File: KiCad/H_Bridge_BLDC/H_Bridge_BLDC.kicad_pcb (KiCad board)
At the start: 2 copper layers, 98 parts, among them J1 DriveCoil, J2 HallDec, J3 Ctrl, J4 12V, Q1 BC32740BU, Q10 BC33740BU, Q11 BC33740BU, Q12 BC33740BU, Q13 BC33740BU, Q14 BC33740BU, Q15 BC33740BU, Q16 BC33740BU, Q17 BC33740BU, Q2 TIP2955G, Q3 TIP3055G, Q4 TIP3055G, Q5 TIP2955G, Q6 BC32740BU, Q9 BC33740BU, U1 VO615A, U2 L7805CV, U3 CD74HC238E, U4 VO615A, U6 LM555xM, U7 LM555xM

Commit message: First version
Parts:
- added C16: 100n, Capacitor_THT:C_Disc_D4.7mm_W2.5mm_P5.00mm, F.Cu at (179.1, 150.4)
- added D18: ZY24 24V / 2W, Diode_THT:D_DO-41_SOD81_P10.16mm_Horizontal, F.Cu at (251.7, 174.3)
- added D19: 20V 1N5250B, Diode_THT:D_DO-35_SOD27_P10.16mm_Horizontal, F.Cu at (239.8, 153.8)
- added D20: 1N5408, Diode_THT:D_DO-201AD_P15.24mm_Horizontal, F.Cu at (243.8, 107.1)
- added D21: 1N5408, Diode_THT:D_DO-201AD_P15.24mm_Horizontal, F.Cu at (233.3, 85.4)
- added D22: 1N5408, Diode_THT:D_DO-201AD_P15.24mm_Horizontal, F.Cu at (239.8, 127.1)
- added D23: 1N5408, Diode_THT:D_DO-201AD_P15.24mm_Horizontal, F.Cu at (256.2, 122.0)
- added D24: LED, LED_THT:LED_D5.0mm, F.Cu at (183.5, 235.1)
- added D25: LED, LED_THT:LED_D5.0mm, F.Cu at (175.8, 235.3)
- added J5: Hall In, Connector_PinHeader_2.54mm:PinHeader_1x05_P2.54mm_Vertical, F.Cu at (171.3, 194.2)
- added J6: Hall Out, Connector_PinHeader_2.54mm:PinHeader_1x03_P2.54mm_Vertical, F.Cu at (196.5, 189.2)
- added Q18: 2N5401, Package_TO_SOT_THT:TO-92_Inline, F.Cu at (177.0, 213.7)
- added Q7: 2N5401, Package_TO_SOT_THT:TO-92_Inline, F.Cu at (192.5, 213.5)
- added Q8: 2N5401, Package_TO_SOT_THT:TO-92_Inline, F.Cu at (184.8, 213.6)
- added R12: 10k, Resistor_THT:R_Axial_DIN0207_L6.3mm_D2.5mm_P10.16mm_Horizontal, F.Cu at (237.5, 178.2)
- added R13: 2k2, Resistor_THT:R_Axial_DIN0207_L6.3mm_D2.5mm_P10.16mm_Horizontal, F.Cu at (229.8, 181.2)
- added R14: 1k, Resistor_THT:R_Axial_DIN0207_L6.3mm_D2.5mm_P10.16mm_Horizontal, F.Cu at (229.8, 157.3)
- added R15: 550, Resistor_THT:R_Axial_DIN0207_L6.3mm_D2.5mm_P10.16mm_Horizontal, F.Cu at (175.4, 193.5)
- added R16: 47, Resistor_THT:R_Axial_DIN0207_L6.3mm_D2.5mm_P10.16mm_Horizontal, F.Cu at (191.3, 207.8)
- added R42: 550, Resistor_THT:R_Axial_DIN0207_L6.3mm_D2.5mm_P10.16mm_Horizontal, F.Cu at (175.3, 189.2)
- added R43: 47, Resistor_THT:R_Axial_DIN0207_L6.3mm_D2.5mm_P10.16mm_Horizontal, F.Cu at (183.5, 207.8)
- added R44: 330, Resistor_THT:R_Axial_DIN0207_L6.3mm_D2.5mm_P10.16mm_Horizontal, F.Cu at (183.5, 218.5)
- added R45: 550, Resistor_THT:R_Axial_DIN0207_L6.3mm_D2.5mm_P10.16mm_Horizontal, F.Cu at (175.4, 185.0)
- added R46: 47, Resistor_THT:R_Axial_DIN0207_L6.3mm_D2.5mm_P10.16mm_Horizontal, F.Cu at (175.8, 207.8)
- added R47: 330, Resistor_THT:R_Axial_DIN0207_L6.3mm_D2.5mm_P10.16mm_Horizontal, F.Cu at (175.8, 218.7)
- added REF**: PinHeader_2x15_P2.54mm_Vertical, Connector_PinHeader_2.54mm:PinHeader_2x15_P2.54mm_Vertical, F.Cu at (249.5, 78.5)
- added REF**: PinHeader_2x15_P2.54mm_Vertical, Connector_PinHeader_2.54mm:PinHeader_2x15_P2.54mm_Vertical, F.Cu at (256.4, 78.5)
- added REF**: PinHeader_2x15_P2.54mm_Vertical, Connector_PinHeader_2.54mm:PinHeader_2x15_P2.54mm_Vertical, F.Cu at (263.3, 78.5)
- added REF**: PinHeader_2x15_P2.54mm_Vertical, Connector_PinHeader_2.54mm:PinHeader_2x15_P2.54mm_Vertical, F.Cu at (242.4, 78.5)
- C12: value 470uF 250V -> 100n; footprint footprints:CP_Radial_D25.0mm_P10.00mm_and_5mm -> Capacitor_THT:C_Disc_D4.7mm_W2.5mm_P5.00mm
- C3: footprint Capacitor_THT:CP_Radial_D25.0mm_P10.00mm_SnapIn -> Capacitor_THT:CP_Radial_D10.0mm_P5.00mm
- C4, C5, C6: footprint footprints:CP_Radial_D25.0mm_P10.00mm_and_5mm -> Capacitor_THT:CP_Radial_D10.0mm_P5.00mm
- D1: value GBU6B -> LED; footprint Diode_THT:Diode_Bridge_Vishay_GBU -> LED_THT:LED_D5.0mm
- Q1, Q6: value BC32740BU -> 2N5401
- Q10, Q11, Q12, Q13, Q14, Q15, Q16, Q17, Q9: value BC33740BU -> 2N5551
- Q2, Q5: value TIP2955G -> BDW94C; footprint Package_TO_SOT_THT:TO-247-3_Vertical -> Package_TO_SOT_THT:TO-220-3_Vertical
- Q3, Q4: value TIP3055G -> BDW93C; footprint Package_TO_SOT_THT:TO-247-3_Vertical -> Package_TO_SOT_THT:TO-220-3_Vertical
- U3: footprint footprints:N0016A -> Package_DIP:DIP-16_W7.62mm_LongPads
- moved R24 198.4 mm to (222.2, 167.5), turned to 90 degrees
- moved R27 184.8 mm to (222.0, 174.0), turned to 180 degrees
- moved Q13 183.5 mm to (231.3, 213.6), turned to 180 degrees
- moved Q12 183.5 mm to (238.8, 213.5), turned to 180 degrees
- moved Q14 183.0 mm to (223.3, 213.5), turned to 180 degrees
- moved Q15 182.5 mm to (215.8, 213.6), turned to 180 degrees
- moved R28 181.2 mm to (237.5, 197.3)
- moved Q16 181.1 mm to (207.9, 213.5), turned to 180 degrees
- moved R30 180.9 mm to (229.8, 197.3)
- moved Q17 180.9 mm to (200.2, 213.5), turned to 180 degrees
- moved R32 180.7 mm to (222.0, 197.3)
- moved R29 180.6 mm to (237.5, 228.7)
- moved R31 180.6 mm to (230.0, 228.7)
- moved D12 180.6 mm to (237.5, 232.6)
- moved D13 180.6 mm to (230.0, 232.6)
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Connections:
- C12 pad 1: +12V -> GNDD
- C12 pad 2: GND -> +5V
- D1 pad 1: /BR+ -> GNDD
- D1 pad 2: /C1 -> Net-(D1-A)
- D10 pad 1: Net-(D10-K) -> HALL_ENABLE
- D10 pad 2: unconnected-(D10-A-Pad2) -> Net-(D10-A)
- Q1 pad 1: Net-(Q1-C) -> Net-(Q1-E)
- Q1 pad 3: Net-(Q1-E) -> Net-(Q1-C)
- Q10 pad 1: HALL_ENABLE -> GNDD
- Q10 pad 2: unconnected-(Q10-B-Pad2) -> Net-(Q10-B)
- Q10 pad 3: GNDD -> HALL_ENABLE
- Q11 pad 1: Net-(Q11-C) -> GNDD
- Q11 pad 3: GNDD -> Net-(Q11-C)
- Q12 pad 1: Net-(Q12-C) -> GNDD
- Q12 pad 3: GNDD -> Net-(Q12-C)
- Q13 pad 1: Net-(Q13-C) -> GNDD
- Q13 pad 3: GNDD -> Net-(Q13-C)
- Q14 pad 1: Net-(Q14-C) -> GNDD
- Q14 pad 3: GNDD -> Net-(Q14-C)
- Q15 pad 1: Net-(Q15-C) -> GNDD
- Q15 pad 3: GNDD -> Net-(Q15-C)
- Q16 pad 1: Net-(Q16-C) -> GNDD
- Q16 pad 3: GNDD -> Net-(Q16-C)
- Q17 pad 1: Net-(Q17-C) -> GNDD
- Q17 pad 3: GNDD -> Net-(Q17-C)
- Q6 pad 1: Net-(Q4-B) -> Net-(Q6-E)
- Q6 pad 3: Net-(Q6-E) -> Net-(Q4-B)
- Q9 pad 1: Net-(Q9-C) -> GNDD
- Q9 pad 3: GNDD -> Net-(Q9-C)
- R22 pad 1: Net-(D10-K) -> HALL_1
- R22 pad 2: unconnected-(R22-Pad2) -> Net-(D1-A)
- U3 pad 1: unconnected-(U3-A0-Pad1) -> HALL_1
- U3 pad 2: unconnected-(U3-A1-Pad2) -> HALL_2
- U3 pad 3: unconnected-(U3-A2-Pad3) -> HALL_3
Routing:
- net +5V: track 74.6 -> 374.5 mm
- net /BR+: track 0.00 -> 108.1 mm
- net /C1: track 0.00 -> 108.1 mm
- net +12V: track 21.4 -> 125.3 mm
- net /C2: track 0.00 -> 97.5 mm
- net A: track 0.00 -> 83.9 mm, vias 0 -> 2
- net HALL_ENABLE: track 0.00 -> 79.6 mm, vias 0 -> 1
- net B: track 0.00 -> 62.8 mm, vias 0 -> 2
- net HALL_3: track 0.00 -> 59.8 mm
- net /PowerSupply/VD: track 40.0 -> 98.0 mm
- net HALL_2: track 0.00 -> 53.7 mm
- net HALL_1: track 0.00 -> 51.5 mm
- net /CAP_BANK: track 0.00 -> 43.3 mm
- net /SINGLE_CAP: track 0.00 -> 39.8 mm
- net Net-(Q1-C): track 0.00 -> 36.7 mm
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- added copper zone on B.Cu, net GND
- added copper zone on F.Cu, net GND
- added copper zone on B.Cu, net GNDD
- added copper zone on F.Cu, net GNDD
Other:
- board outline added: 100 x 200 mm
- board text added: "{ "ViaStitching": "0.2", "stitch_zone_0": { "HSpacing": "2.54", "VSpacing": "2.54", "Clearance": "0", "Randomize": false } }"

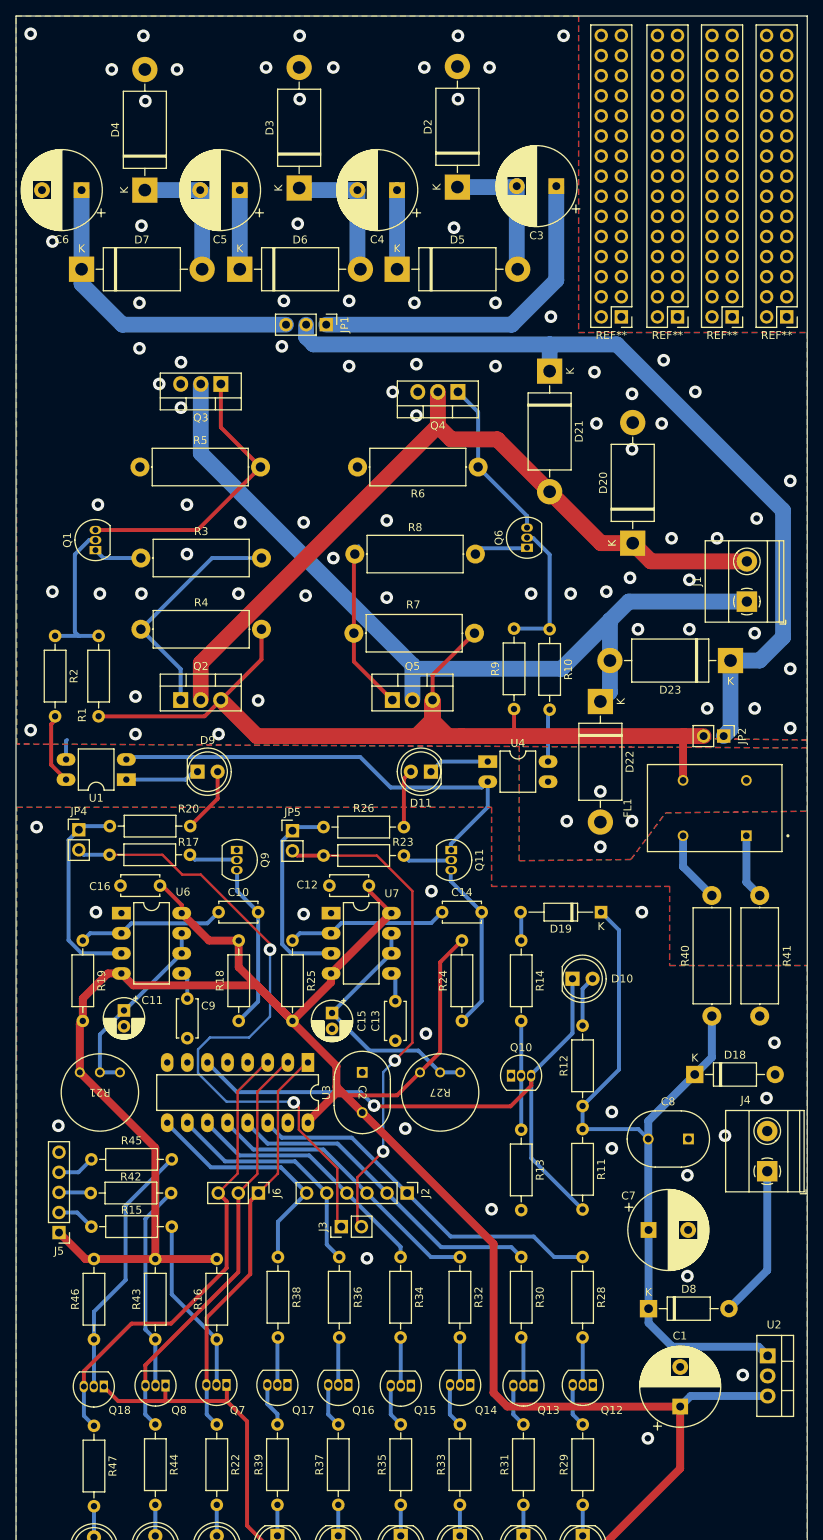
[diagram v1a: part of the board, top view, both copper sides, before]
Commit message: Added mounting holes
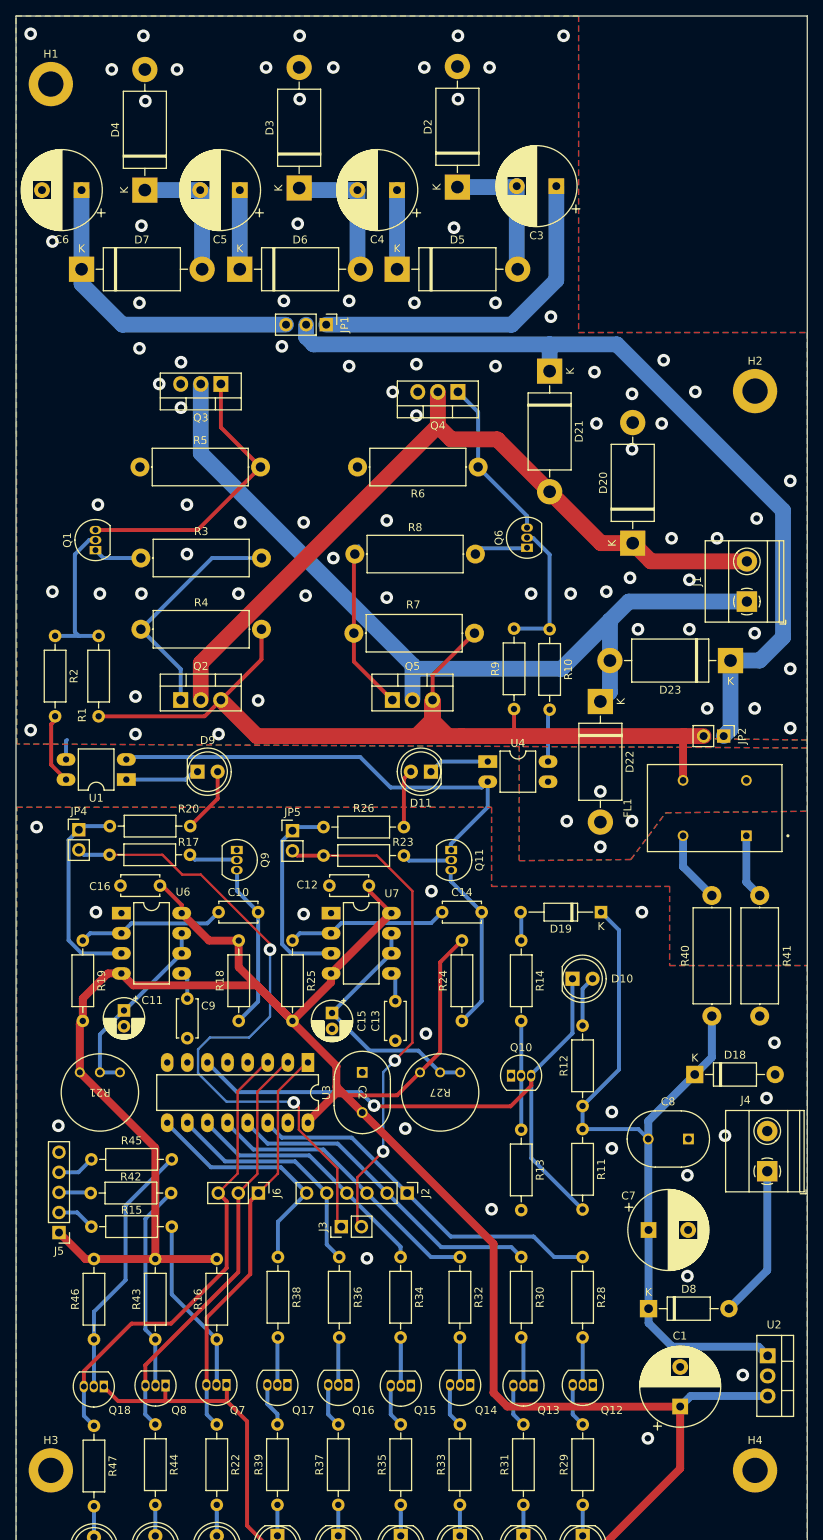
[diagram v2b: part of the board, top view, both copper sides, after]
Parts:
- removed REF** (x4): PinHeader_2x15_P2.54mm_Vertical, Connector_PinHeader_2.54mm:PinHeader_2x15_P2.54mm_Vertical
- added H1: Mounting Hole, MountingHole:MountingHole_3.2mm_M3_DIN965_Pad, F.Cu at (170.3, 49.1)
- added H2: Mounting Hole, MountingHole:MountingHole_3.2mm_M3_DIN965_Pad, F.Cu at (259.3, 87.9)
- added H3: Mounting Hole, MountingHole:MountingHole_3.2mm_M3_DIN965_Pad, F.Cu at (170.3, 224.3)
- added H4: Mounting Hole, MountingHole:MountingHole_3.2mm_M3_DIN965_Pad, F.Cu at (259.3, 224.3)

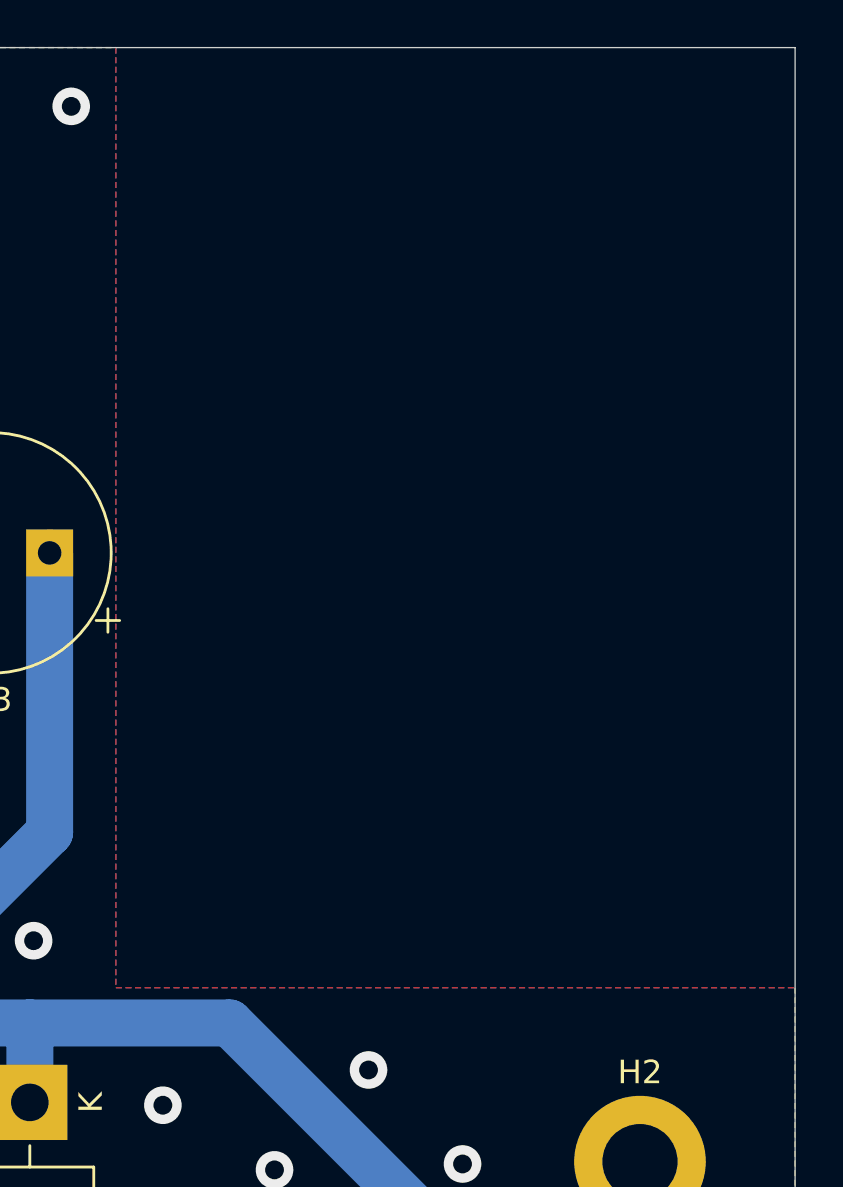
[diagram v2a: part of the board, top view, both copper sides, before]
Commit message: Added some connectors for expermental area
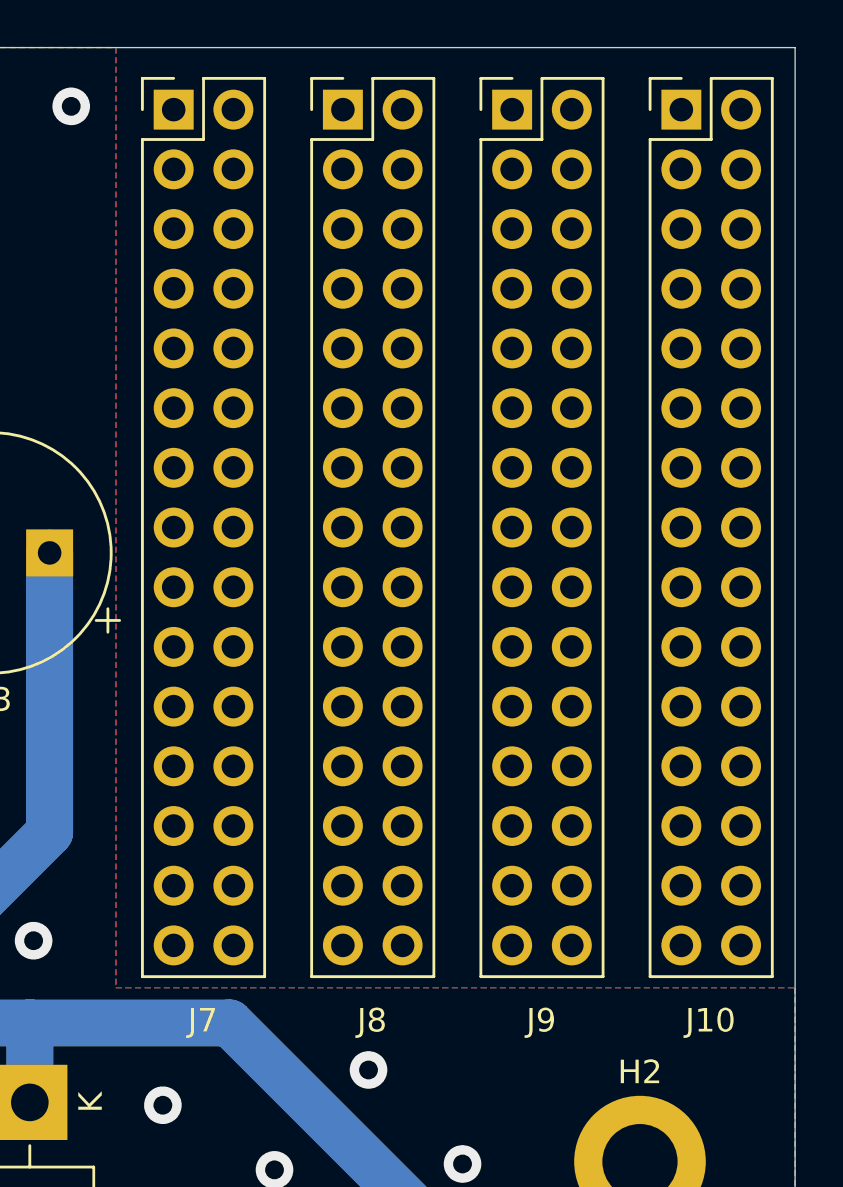
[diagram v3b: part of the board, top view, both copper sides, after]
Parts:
- added J10: Conn_02x15_Counter_Clockwise, Connector_PinHeader_2.54mm:PinHeader_2x15_P2.54mm_Vertical, F.Cu at (261.1, 43.1)
- added J7: Conn_02x15_Counter_Clockwise, Connector_PinHeader_2.54mm:PinHeader_2x15_P2.54mm_Vertical, F.Cu at (239.5, 43.1)
- added J8: Conn_02x15_Counter_Clockwise, Connector_PinHeader_2.54mm:PinHeader_2x15_P2.54mm_Vertical, F.Cu at (246.7, 43.1)
- added J9: Conn_02x15_Counter_Clockwise, Connector_PinHeader_2.54mm:PinHeader_2x15_P2.54mm_Vertical, F.Cu at (253.9, 43.1)
